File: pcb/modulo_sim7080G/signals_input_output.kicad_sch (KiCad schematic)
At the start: 12 parts, among them Q1 BC846, SW1 SW_Push, U2 PDTC114EU, U4 PDTC114EU

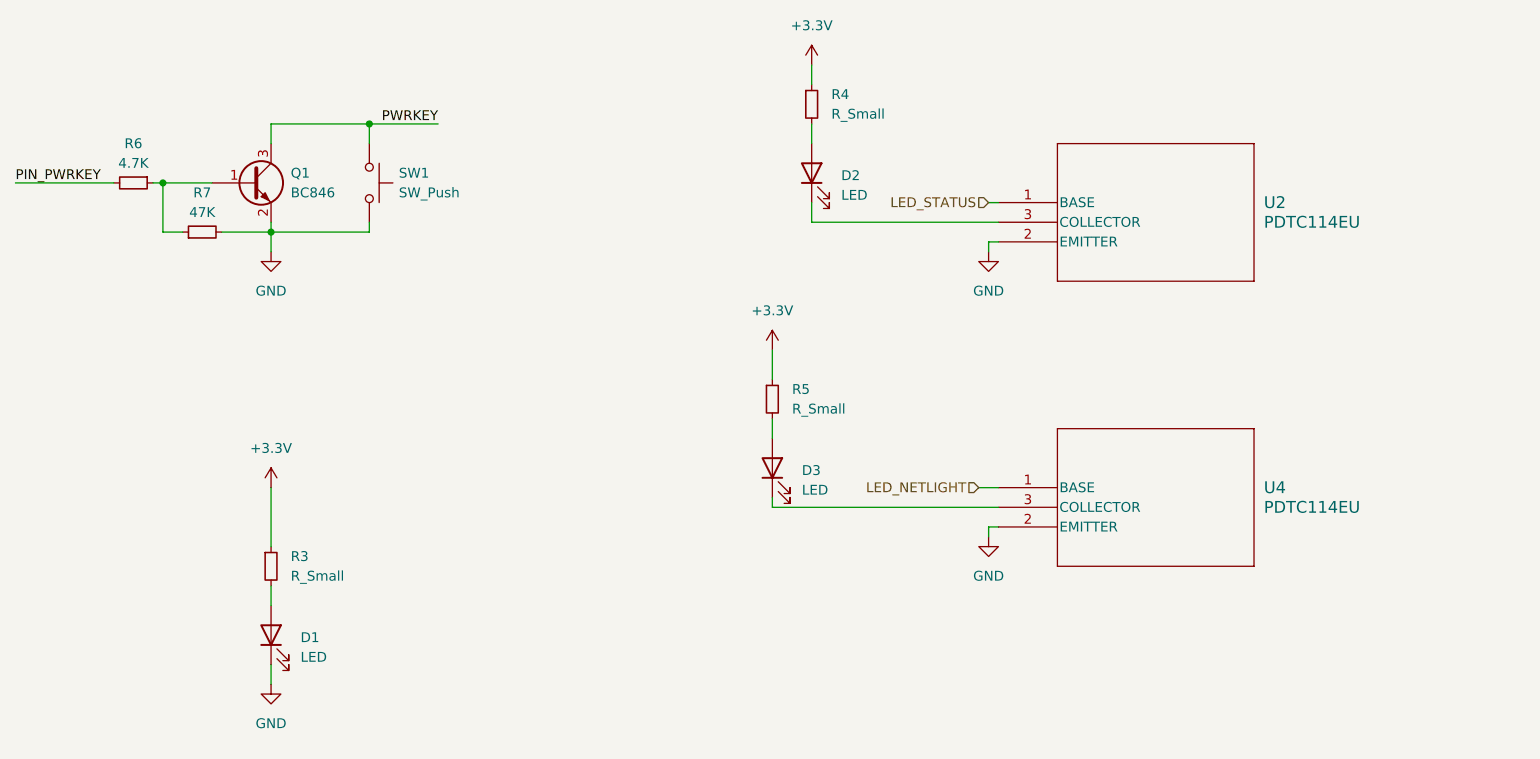
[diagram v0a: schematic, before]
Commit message: se ordenaron los componentes en el pcb
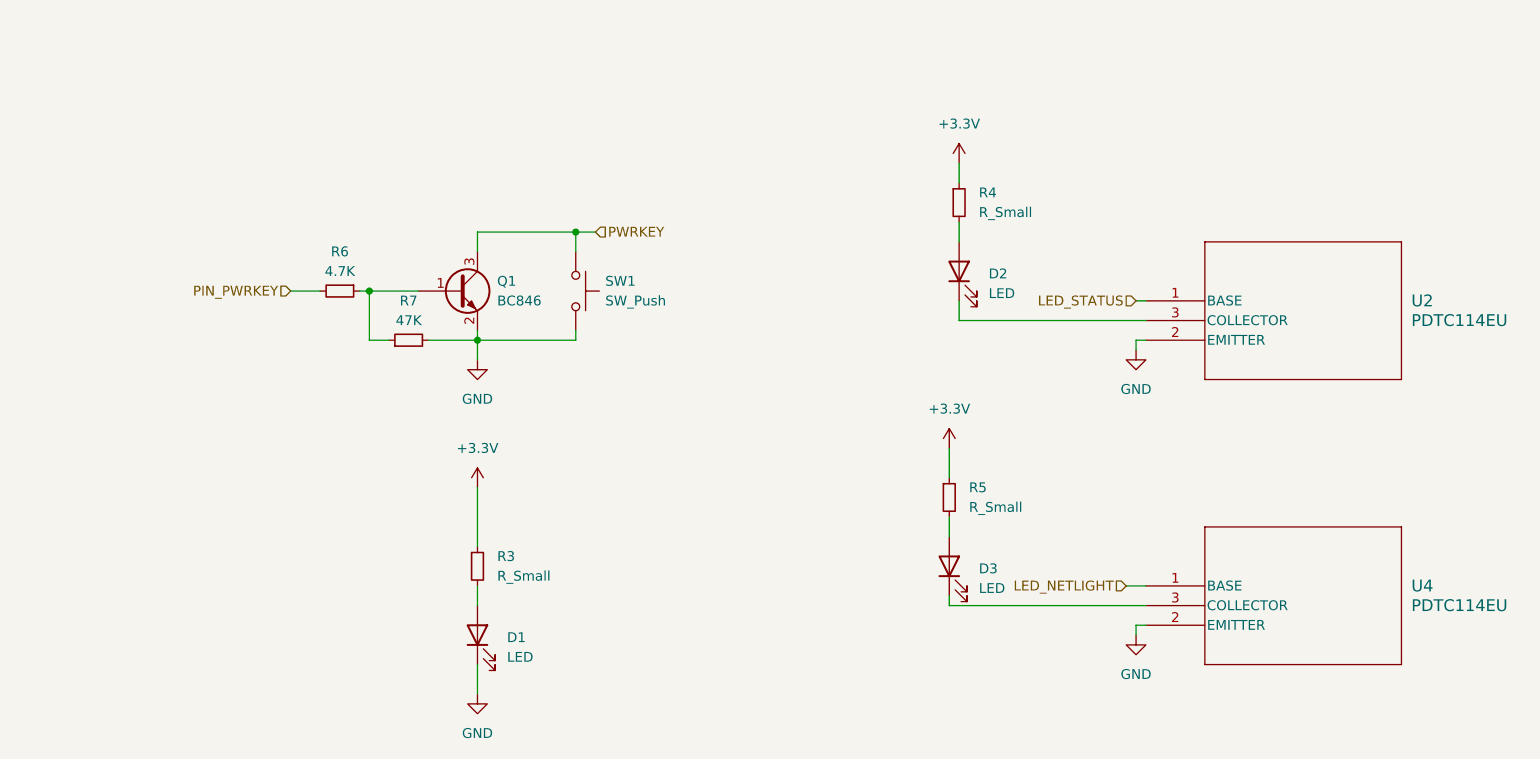
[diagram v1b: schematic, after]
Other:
- moved on the sheet: D1, D2, D3, Q1, R3, R4, R5, R6, R7, SW1, U2, U4
